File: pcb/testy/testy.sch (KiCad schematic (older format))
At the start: 76 parts, among them J1 L_XLED, J2 R_XLED, J3 SLAVE_LED, P1 OLED, P2 ICSP, SW0:0 SW_Push, SW0:1 SW_Push, SW0:2 SW_Push, SW0:3 SW_Push, SW0:4 SW_Push, SW1:0 SW_Push, SW1:1 SW_Push, SW1:2 SW_Push, SW1:3 SW_Push, SW1:4 SW_Push, SW2:0 SW_Push, SW2:1 SW_Push, SW2:2 SW_Push, SW2:3 SW_Push, SW2:4 SW_Push, SW3:0 SW_Push, SW3:1 SW_Push, SW3:2 SW_Push, SW3:3 SW_Push, SW3:4 SW_Push, SW3:5 SW_Push, SW4:1 SW_Push, SW4:2 SW_Push, SW4:3 SW_Push, SW4:4 SW_Push, SW4:5 SW_Push

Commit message: feat: create a choc-only footprint and use that for the bottom row, check that making the other switches MX only will remove DRC errors and it will, so that needs to be done. Also add choc reference PDF
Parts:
- SW3:5: footprint footprints:kailh-socket-and-choc-solder-reversible -> footprints:Kailh_socket_reversible
- SW4:1, SW4:2, SW4:3, SW4:4, SW4:5: footprint footprints:kailh-socket-and-choc-solder-reversible -> footprints:kailh-choc-solder-reversible
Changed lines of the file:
@@
 F 0 "SW3:5" H 9150 3935 50  0000 C CNN
 F 1 "SW_Push" H 9150 3844 50  0000 C CNN
-F 2 "footprints:kailh-socket-and-choc-solder-reversible" H 9150 3850 50  0001 C CNN
+F 2 "footprints:Kailh_socket_reversible" H 9150 3850 50  0001 C CNN
 F 3 "~" H 9150 3850 50  0001 C CNN
 	1    9150 3650
@@
 F 0 "SW4:1" H 5450 4635 50  0000 C CNN
 F 1 "SW_Push" H 5450 4544 50  0000 C CNN
-F 2 "footprints:kailh-socket-and-choc-solder-reversible" H 5450 4550 50  0001 C CNN
+F 2 "footprints:kailh-choc-solder-reversible" H 5450 4550 50  0001 C CNN
 F 3 "~" H 5450 4550 50  0001 C CNN
 	1    5450 4350
@@
 F 0 "SW4:2" H 6350 4635 50  0000 C CNN
 F 1 "SW_Push" H 6350 4544 50  0000 C CNN
-F 2 "footprints:kailh-socket-and-choc-solder-reversible" H 6350 4550 50  0001 C CNN
+F 2 "footprints:kailh-choc-solder-reversible" H 6350 4550 50  0001 C CNN
 F 3 "~" H 6350 4550 50  0001 C CNN
 	1    6350 4350
@@
 F 0 "SW4:3" H 7250 4635 50  0000 C CNN
 F 1 "SW_Push" H 7250 4544 50  0000 C CNN
-F 2 "footprints:kailh-socket-and-choc-solder-reversible" H 7250 4550 50  0001 C CNN
+F 2 "footprints:kailh-choc-solder-reversible" H 7250 4550 50  0001 C CNN
 F 3 "~" H 7250 4550 50  0001 C CNN
 	1    7250 4350
@@
 F 0 "SW4:4" H 8250 4635 50  0000 C CNN
 F 1 "SW_Push" H 8250 4544 50  0000 C CNN
-F 2 "footprints:kailh-socket-and-choc-solder-reversible" H 8250 4550 50  0001 C CNN
+F 2 "footprints:kailh-choc-solder-reversible" H 8250 4550 50  0001 C CNN
 F 3 "~" H 8250 4550 50  0001 C CNN
 	1    8250 4350
@@
 F 0 "SW4:5" H 9150 4635 50  0000 C CNN
 F 1 "SW_Push" H 9150 4544 50  0000 C CNN
-F 2 "footprints:kailh-socket-and-choc-solder-reversible" H 9150 4550 50  0001 C CNN
+F 2 "footprints:kailh-choc-solder-reversible" H 9150 4550 50  0001 C CNN
 F 3 "~" H 9150 4550 50  0001 C CNN
 	1    9150 4350

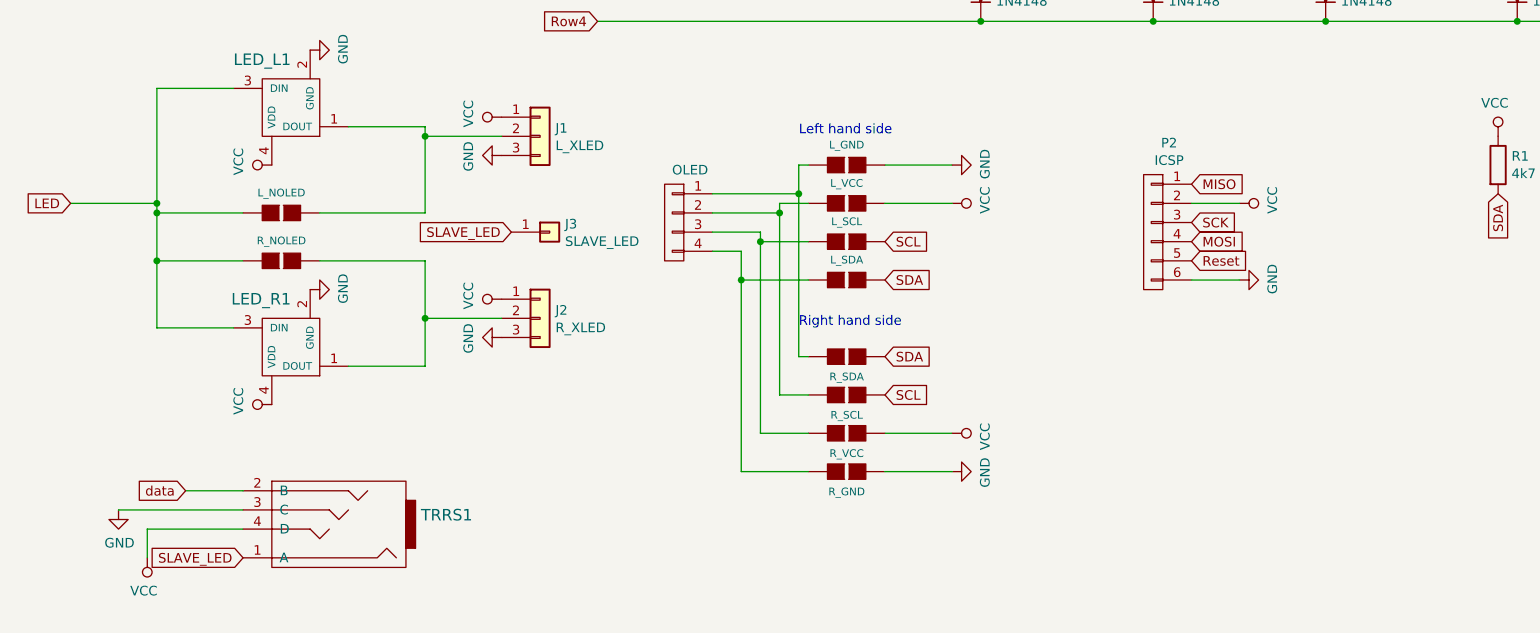
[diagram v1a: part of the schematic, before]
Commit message: feat: add back LED bypass jumpers
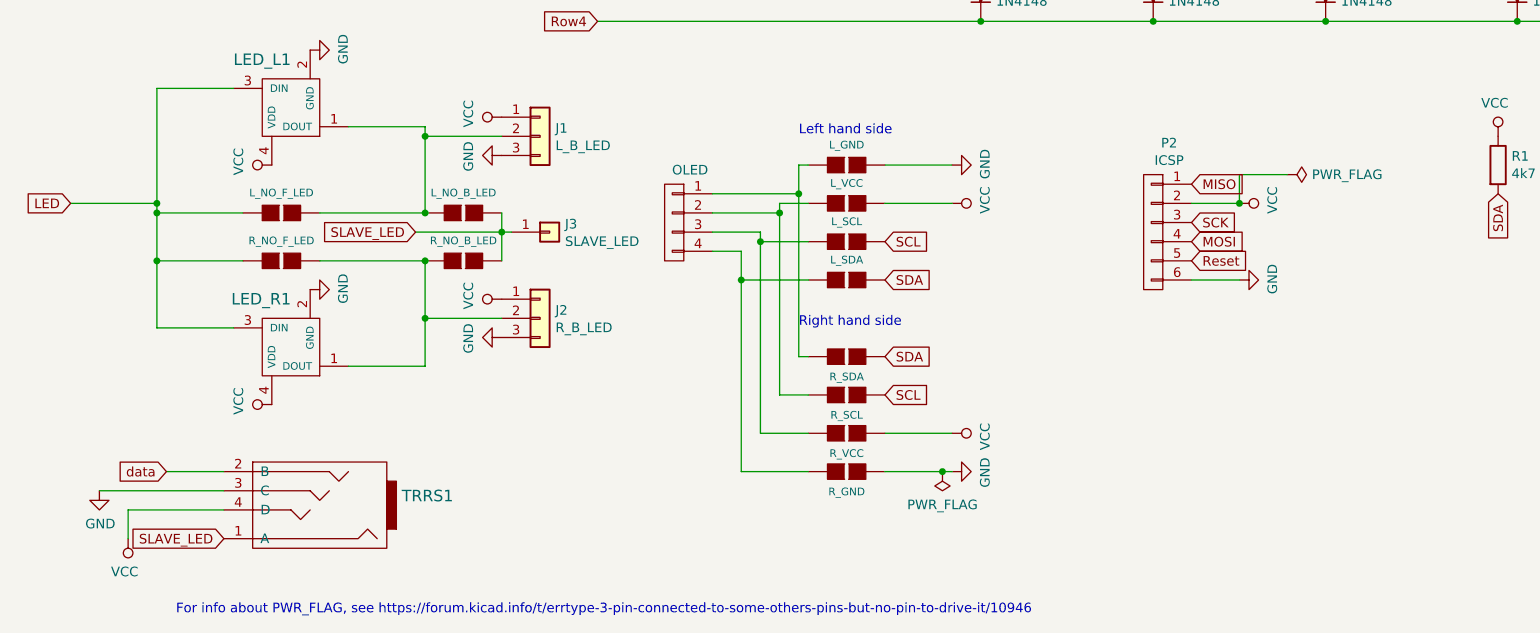
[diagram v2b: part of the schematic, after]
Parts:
- added JP10: L_NO_B_LED, footprints:Jumper, symbol jp2:JP2
- added JP11: R_NO_B_LED, footprints:Jumper, symbol jp2:JP2
- J1: value L_XLED -> L_B_LED
- J2: value R_XLED -> R_B_LED
- JP12: value R_NOLED -> R_NO_F_LED
- JP9: value L_NOLED -> L_NO_F_LED
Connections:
- net SLAVE_LED: now also JP10.1 (G1), JP11.1 (G1)
- net at J1.2 (Pin_2), JP9.1 (G1), LED_L1.1 (DOUT): now also JP10.2 (G2)
- net at J2.2 (Pin_2), JP12.1 (G1), LED_R1.1 (DOUT): now also JP11.2 (G2)
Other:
- note added: "For info about PWR_FLAG, see https://forum.kicad.info/t/errtype-3-pin-connected-to-some-others-pins-but-no-pin-to-drive-it/10946"
- moved on the sheet: TRRS1

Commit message: feat: update all MX switches to MX-only footprint, still need to update edge cuts
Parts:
- SW0:0, SW0:1, SW0:2, SW0:3, SW0:4, SW1:0, SW1:1, SW1:2, SW1:3, SW1:4, SW2:0, SW2:1, SW2:2, SW2:3, SW2:4, SW3:0, SW3:1, SW3:2, SW3:3, SW3:4: footprint footprints:kailh-socket-and-choc-solder-reversible -> footprints:Kailh_socket_reversible
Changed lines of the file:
@@
 F 0 "SW0:1" H 5450 1835 50  0000 C CNN
 F 1 "SW_Push" H 5450 1744 50  0000 C CNN
-F 2 "footprints:kailh-socket-and-choc-solder-reversible" H 5450 1750 50  0001 C CNN
+F 2 "footprints:Kailh_socket_reversible" H 5450 1750 50  0001 C CNN
 F 3 "~" H 5450 1750 50  0001 C CNN
 	1    5450 1550
@@
 F 0 "SW0:2" H 6350 1835 50  0000 C CNN
 F 1 "SW_Push" H 6350 1744 50  0000 C CNN
-F 2 "footprints:kailh-socket-and-choc-solder-reversible" H 6350 1750 50  0001 C CNN
+F 2 "footprints:Kailh_socket_reversible" H 6350 1750 50  0001 C CNN
 F 3 "~" H 6350 1750 50  0001 C CNN
 	1    6350 1550
@@
 F 0 "SW1:1" H 5450 2535 50  0000 C CNN
 F 1 "SW_Push" H 5450 2444 50  0000 C CNN
-F 2 "footprints:kailh-socket-and-choc-solder-reversible" H 5450 2450 50  0001 C CNN
+F 2 "footprints:Kailh_socket_reversible" H 5450 2450 50  0001 C CNN
 F 3 "~" H 5450 2450 50  0001 C CNN
 	1    5450 2250
@@
 F 0 "SW1:2" H 6350 2535 50  0000 C CNN
 F 1 "SW_Push" H 6350 2444 50  0000 C CNN
-F 2 "footprints:kailh-socket-and-choc-solder-reversible" H 6350 2450 50  0001 C CNN
+F 2 "footprints:Kailh_socket_reversible" H 6350 2450 50  0001 C CNN
 F 3 "~" H 6350 2450 50  0001 C CNN
 	1    6350 2250
@@
 F 0 "SW0:3" H 7250 1835 50  0000 C CNN
 F 1 "SW_Push" H 7250 1744 50  0000 C CNN
-F 2 "footprints:kailh-socket-and-choc-solder-reversible" H 7250 1750 50  0001 C CNN
+F 2 "footprints:Kailh_socket_reversible" H 7250 1750 50  0001 C CNN
 F 3 "~" H 7250 1750 50  0001 C CNN
 	1    7250 1550
@@
 F 0 "SW1:3" H 7250 2535 50  0000 C CNN
 F 1 "SW_Push" H 7250 2444 50  0000 C CNN
-F 2 "footprints:kailh-socket-and-choc-solder-reversible" H 7250 2450 50  0001 C CNN
+F 2 "footprints:Kailh_socket_reversible" H 7250 2450 50  0001 C CNN
 F 3 "~" H 7250 2450 50  0001 C CNN
 	1    7250 2250
@@
 F 0 "SW2:1" H 5450 3235 50  0000 C CNN
 F 1 "SW_Push" H 5450 3144 50  0000 C CNN
-F 2 "footprints:kailh-socket-and-choc-solder-reversible" H 5450 3150 50  0001 C CNN
+F 2 "footprints:Kailh_socket_reversible" H 5450 3150 50  0001 C CNN
 F 3 "~" H 5450 3150 50  0001 C CNN
 	1    5450 2950
@@
 F 0 "SW2:2" H 6350 3235 50  0000 C CNN
 F 1 "SW_Push" H 6350 3144 50  0000 C CNN
-F 2 "footprints:kailh-socket-and-choc-solder-reversible" H 6350 3150 50  0001 C CNN
+F 2 "footprints:Kailh_socket_reversible" H 6350 3150 50  0001 C CNN
 F 3 "~" H 6350 3150 50  0001 C CNN
 	1    6350 2950
@@
 F 0 "SW3:1" H 5450 3935 50  0000 C CNN
 F 1 "SW_Push" H 5450 3844 50  0000 C CNN
-F 2 "footprints:kailh-socket-and-choc-solder-reversible" H 5450 3850 50  0001 C CNN
+F 2 "footprints:Kailh_socket_reversible" H 5450 3850 50  0001 C CNN
 F 3 "~" H 5450 3850 50  0001 C CNN
 	1    5450 3650
@@
 F 0 "SW3:2" H 6350 3935 50  0000 C CNN
 F 1 "SW_Push" H 6350 3844 50  0000 C CNN
-F 2 "footprints:kailh-socket-and-choc-solder-reversible" H 6350 3850 50  0001 C CNN
+F 2 "footprints:Kailh_socket_reversible" H 6350 3850 50  0001 C CNN
 F 3 "~" H 6350 3850 50  0001 C CNN
 	1    6350 3650
@@
 F 0 "SW2:3" H 7250 3235 50  0000 C CNN
 F 1 "SW_Push" H 7250 3144 50  0000 C CNN
-F 2 "footprints:kailh-socket-and-choc-solder-reversible" H 7250 3150 50  0001 C CNN
+F 2 "footprints:Kailh_socket_reversible" H 7250 3150 50  0001 C CNN
 F 3 "~" H 7250 3150 50  0001 C CNN
 	1    7250 2950
@@
 F 0 "SW3:3" H 7250 3935 50  0000 C CNN
 F 1 "SW_Push" H 7250 3844 50  0000 C CNN
-F 2 "footprints:kailh-socket-and-choc-solder-reversible" H 7250 3850 50  0001 C CNN
+F 2 "footprints:Kailh_socket_reversible" H 7250 3850 50  0001 C CNN
 F 3 "~" H 7250 3850 50  0001 C CNN
 	1    7250 3650
@@
 F 0 "SW0:4" H 8250 1835 50  0000 C CNN
 F 1 "SW_Push" H 8250 1744 50  0000 C CNN
-F 2 "footprints:kailh-socket-and-choc-solder-reversible" H 8250 1750 50  0001 C CNN
+F 2 "footprints:Kailh_socket_reversible" H 8250 1750 50  0001 C CNN
 F 3 "~" H 8250 1750 50  0001 C CNN
 	1    8250 1550
@@
 F 0 "SW1:4" H 8250 2535 50  0000 C CNN
 F 1 "SW_Push" H 8250 2444 50  0000 C CNN
-F 2 "footprints:kailh-socket-and-choc-solder-reversible" H 8250 2450 50  0001 C CNN
+F 2 "footprints:Kailh_socket_reversible" H 8250 2450 50  0001 C CNN
 F 3 "~" H 8250 2450 50  0001 C CNN
 	1    8250 2250
@@
 F 0 "SW2:4" H 8250 3235 50  0000 C CNN
 F 1 "SW_Push" H 8250 3144 50  0000 C CNN
-F 2 "footprints:kailh-socket-and-choc-solder-reversible" H 8250 3150 50  0001 C CNN
+F 2 "footprints:Kailh_socket_reversible" H 8250 3150 50  0001 C CNN
 F 3 "~" H 8250 3150 50  0001 C CNN
 	1    8250 2950
@@
 F 0 "SW3:4" H 8250 3935 50  0000 C CNN
 F 1 "SW_Push" H 8250 3844 50  0000 C CNN
-F 2 "footprints:kailh-socket-and-choc-solder-reversible" H 8250 3850 50  0001 C CNN
+F 2 "footprints:Kailh_socket_reversible" H 8250 3850 50  0001 C CNN
 F 3 "~" H 8250 3850 50  0001 C CNN
 	1    8250 3650
@@
 F 0 "SW3:0" H 4450 3935 50  0000 C CNN
 F 1 "SW_Push" H 4450 3844 50  0000 C CNN
-F 2 "footprints:kailh-socket-and-choc-solder-reversible" H 4450 3850 50  0001 C CNN
+F 2 "footprints:Kailh_socket_reversible" H 4450 3850 50  0001 C CNN
 F 3 "~" H 4450 3850 50  0001 C CNN
 	1    4450 3650
@@
 F 0 "SW2:0" H 4450 3235 50  0000 C CNN
 F 1 "SW_Push" H 4450 3144 50  0000 C CNN
-F 2 "footprints:kailh-socket-and-choc-solder-reversible" H 4450 3150 50  0001 C CNN
+F 2 "footprints:Kailh_socket_reversible" H 4450 3150 50  0001 C CNN
 F 3 "~" H 4450 3150 50  0001 C CNN
 	1    4450 2950
@@
 F 0 "SW1:0" H 4450 2535 50  0000 C CNN
 F 1 "SW_Push" H 4450 2444 50  0000 C CNN
-F 2 "footprints:kailh-socket-and-choc-solder-reversible" H 4450 2450 50  0001 C CNN
+F 2 "footprints:Kailh_socket_reversible" H 4450 2450 50  0001 C CNN
 F 3 "~" H 4450 2450 50  0001 C CNN
 	1    4450 2250
@@
 F 0 "SW0:0" H 4450 1835 50  0000 C CNN
 F 1 "SW_Push" H 4450 1744 50  0000 C CNN
-F 2 "footprints:kailh-socket-and-choc-solder-reversible" H 4450 1750 50  0001 C CNN
+F 2 "footprints:Kailh_socket_reversible" H 4450 1750 50  0001 C CNN
 F 3 "~" H 4450 1750 50  0001 C CNN
 	1    4450 1550
